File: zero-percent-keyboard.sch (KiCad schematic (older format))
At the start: 195 parts, among them J1 USB4085-GF-A_REVA, SW1 SW_PUSH, U1 ATMEGA32U4, X1 XTAL_GND

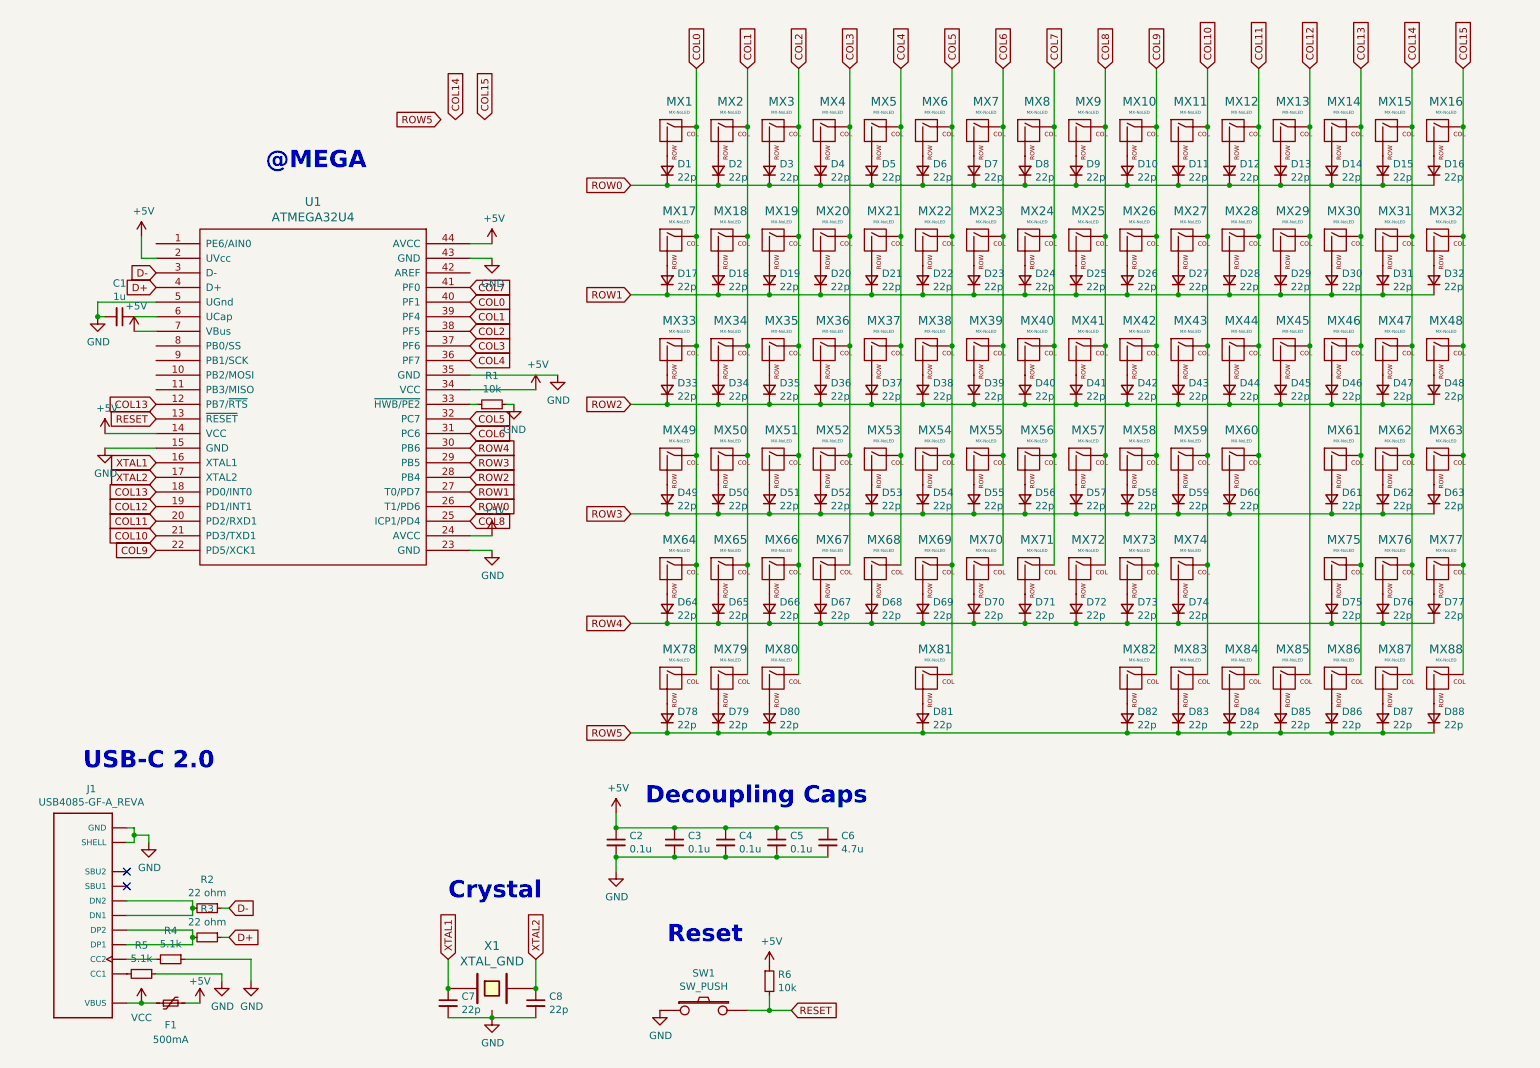
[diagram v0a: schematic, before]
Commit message: Layout change
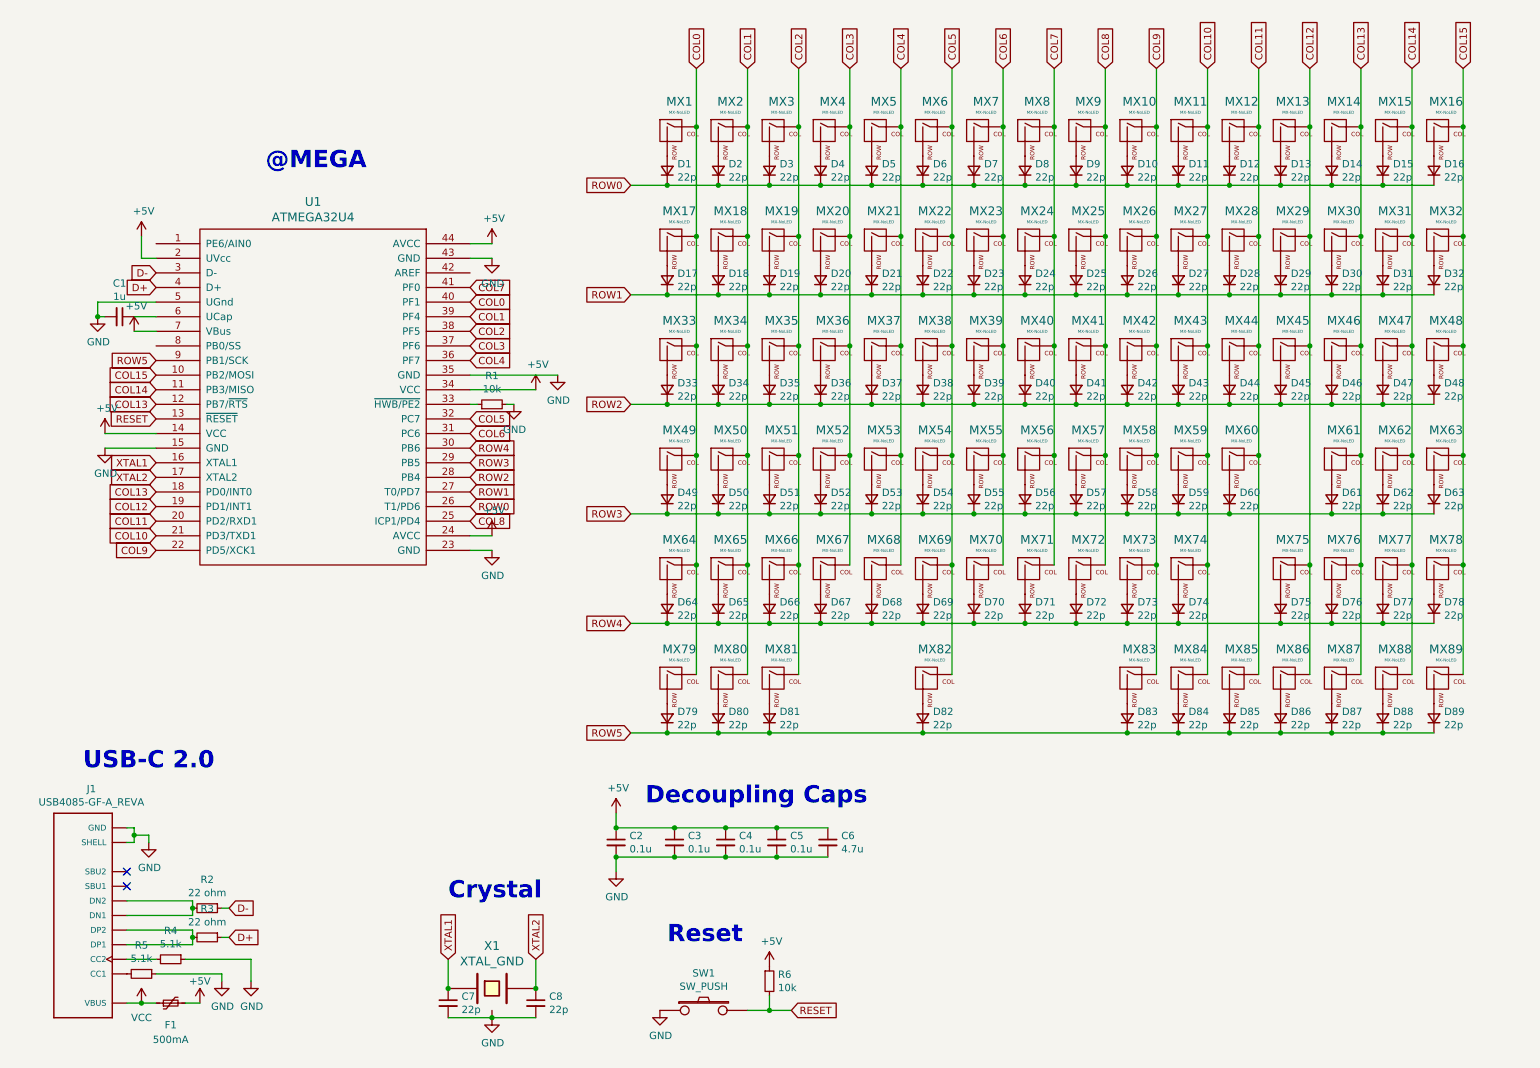
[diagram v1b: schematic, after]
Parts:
- added D75: 22p, Diode_SMD:D_SOD-123, symbol Device:D_Small
- added MX75: MX-NoLED, MX_Only:MXOnly-1.75U-NoLED, symbol MX_Alps_Hybrid:MX-NoLED
- MX17, MX43, MX51, MX52, MX53, MX55, MX56, MX57, MX58, MX65, MX66, MX67, MX68, MX69, MX70, MX71, MX72, MX73, MX74: footprint MX_Only:MXOnly-1.25U-NoLED -> MX_Only:MXOnly-1U-NoLED
- MX28: footprint MX_Only:MXOnly-1.75U-NoLED -> MX_Only:MXOnly-1U-NoLED
- MX30: footprint MX_Only:MXOnly-1U-NoLED -> MX_Only:MXOnly-2U-NoLED
- MX33: footprint MX_Only:MXOnly-1.75U-NoLED -> MX_Only:MXOnly-1.5U-NoLED
- MX46: footprint MX_Only:MXOnly-1U-NoLED -> MX_Only:MXOnly-1.5U-NoLED
- MX49: footprint MX_Only:MXOnly-1.25U-NoLED -> MX_Only:MXOnly-1.75U-NoLED
- MX54: footprint MX_Only:MXOnly-6.25U-ReversedStabilizers-NoLED -> MX_Only:MXOnly-1U-NoLED
- MX61: footprint MX_Only:MXOnly-1U-NoLED -> MX_Only:MXOnly-2.25U-NoLED
- MX64: footprint MX_Only:MXOnly-1.25U-NoLED -> MX_Only:MXOnly-2.25U-NoLED
- MX76: renamed from MX75; footprint MX_Only:MXOnly-1.25U-NoLED -> MX_Only:MXOnly-1U-NoLED
- MX77: renamed from MX76; footprint MX_Only:MXOnly-1.25U-NoLED -> MX_Only:MXOnly-1U-NoLED
- MX78: renamed from MX77; footprint MX_Only:MXOnly-1.25U-NoLED -> MX_Only:MXOnly-1U-NoLED
- MX82: renamed from MX81; footprint MX_Only:MXOnly-1.25U-NoLED -> MX_Only:MXOnly-6.25U-ReversedStabilizers-NoLED
- MX83: renamed from MX82; footprint MX_Only:MXOnly-1.25U-NoLED -> MX_Only:MXOnly-1U-NoLED
- MX84: renamed from MX83; footprint MX_Only:MXOnly-1.25U-NoLED -> MX_Only:MXOnly-1U-NoLED
- MX85: renamed from MX84; footprint MX_Only:MXOnly-1.25U-NoLED -> MX_Only:MXOnly-1U-NoLED
- MX86: renamed from MX85; footprint MX_Only:MXOnly-1.25U-NoLED -> MX_Only:MXOnly-1U-NoLED
- MX87: renamed from MX86; footprint MX_Only:MXOnly-1.25U-NoLED -> MX_Only:MXOnly-1U-NoLED
- MX88: renamed from MX87; footprint MX_Only:MXOnly-1.25U-NoLED -> MX_Only:MXOnly-1U-NoLED
- MX89: renamed from MX88; footprint MX_Only:MXOnly-1.25U-NoLED -> MX_Only:MXOnly-1U-NoLED
- renumbered D75 to D76, D76 to D77, D77 to D78, D78 to D79, D79 to D80, D80 to D81, D81 to D82, D82 to D83, D83 to D84, D84 to D85, D85 to D86, D86 to D87, D87 to D88, D88 to D89, MX78 to MX79, MX79 to MX80, MX80 to MX81
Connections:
- net COL12: now also MX75.1 (COL)
- net COL14: now also U1.11 (PB3/MISO)
- net COL15: now also U1.10 (PB2/MOSI)
- net ROW4: now also D75.1 (K)
- net ROW5: now also U1.9 (PB1/SCK)
- new net: D75.2 (A), MX75.2 (ROW)

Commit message: Route traces
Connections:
- net COL0: now also U1.31 (PC6); no longer U1.40 (PF1)
- net COL1: now also U1.32 (PC7); no longer U1.39 (PF4)
- net COL5: no longer U1.32 (PC7)
- net COL6: no longer U1.31 (PC6)
- net COL8: no longer U1.25 (ICP1/PD4)
- net ROW5: now also U1.25 (ICP1/PD4); no longer U1.9 (PB1/SCK)
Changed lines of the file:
@@
 Text GLabel 3850 2400 2    50   Input ~ 0
 COL7
-Text GLabel 3850 3400 2    50   Input ~ 0
+Text GLabel 4250 2650 2    50   Input ~ 0
 COL6
-Text GLabel 3850 3300 2    50   Input ~ 0
+Text GLabel 4250 2550 2    50   Input ~ 0
 COL5
 Text GLabel 3850 2900 2    50   Input ~ 0
@@
 Text GLabel 3850 3700 2    50   Input ~ 0
 ROW2
-Text GLabel 3850 2600 2    50   Input ~ 0
+Text GLabel 3850 3300 2    50   Input ~ 0
 COL1
-Text GLabel 3850 2500 2    50   Input ~ 0
+Text GLabel 3850 3400 2    50   Input ~ 0
 COL0
-Text GLabel 3850 4000 2    50   Input ~ 0
+Text GLabel 1400 2900 2    50   Input ~ 0
 COL8
 Text GLabel 1700 4200 0    50   Input ~ 0
@@
 Text GLabel 3850 3500 2    50   Input ~ 0
 ROW4
-Text GLabel 1700 2900 0    50   Input ~ 0
+Text GLabel 3850 4000 2    50   Input ~ 0
 ROW5
 $Comp

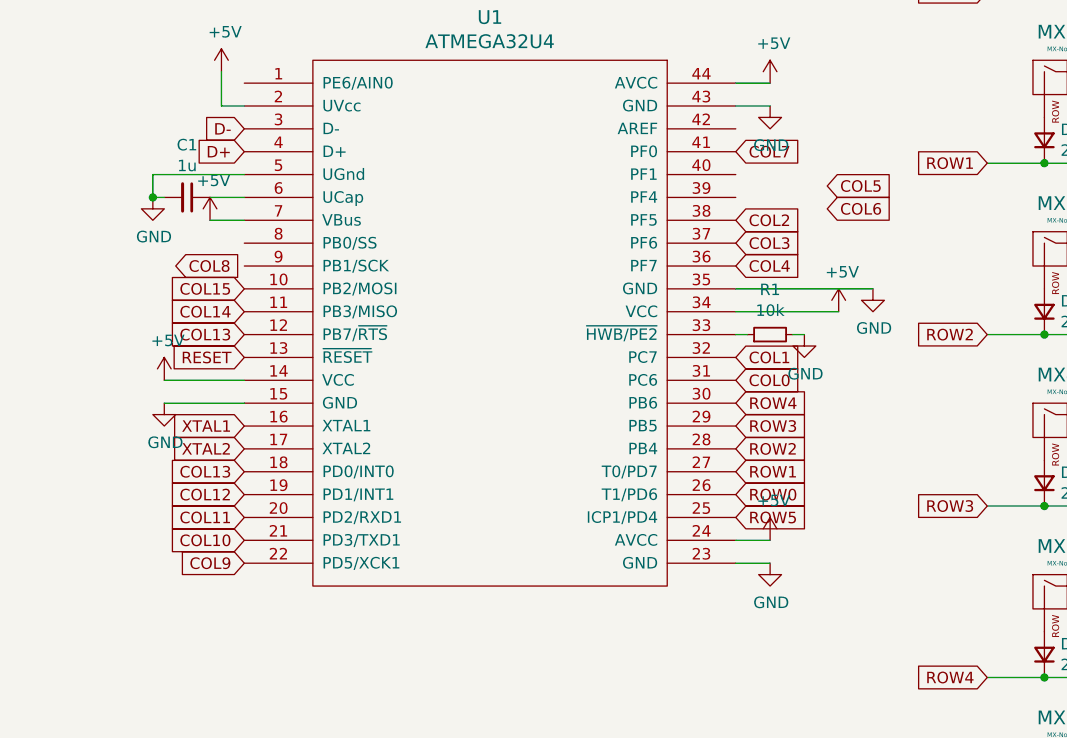
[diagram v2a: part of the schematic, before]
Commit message: Rearrange rows and columns in schematic
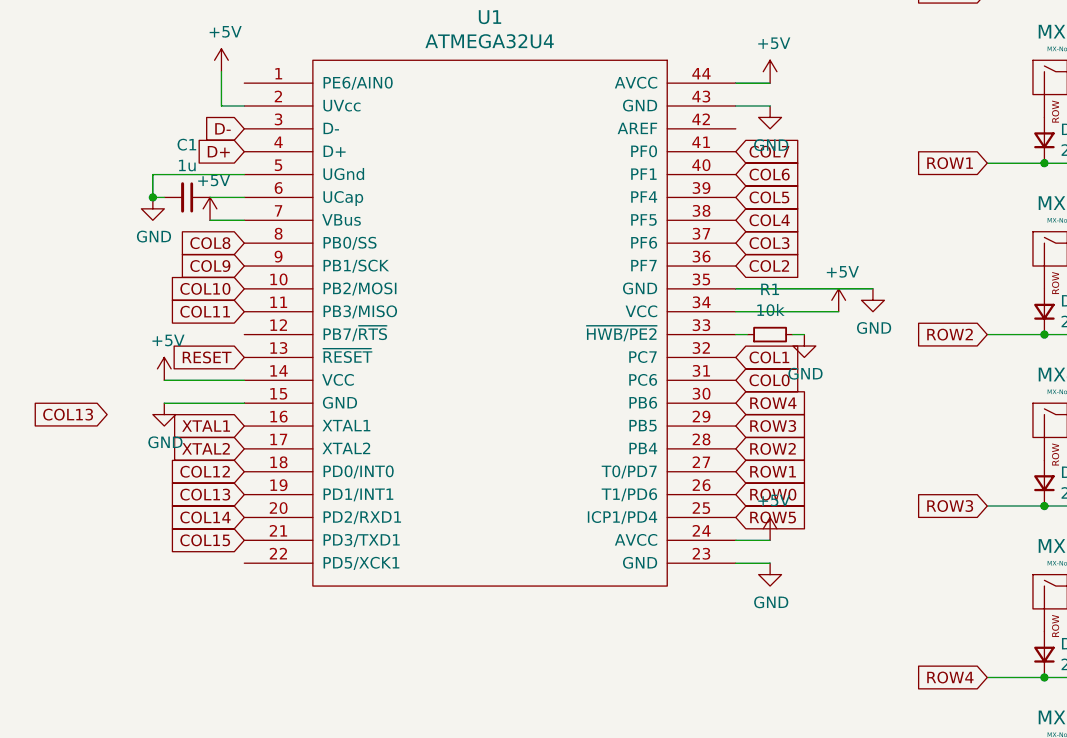
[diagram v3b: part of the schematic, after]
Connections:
- net COL10: now also U1.10 (PB2/MOSI); no longer U1.21 (PD3/TXD1)
- net COL11: now also U1.11 (PB3/MISO); no longer U1.20 (PD2/RXD1)
- net COL12: now also U1.18 (PD0/INT0); no longer U1.19 (PD1/INT1)
- net COL13: now also U1.19 (PD1/INT1); no longer U1.12 (PB7/~RTS), U1.18 (PD0/INT0)
- net COL14: now also U1.20 (PD2/RXD1); no longer U1.11 (PB3/MISO)
- net COL15: now also U1.21 (PD3/TXD1); no longer U1.10 (PB2/MOSI)
- net COL2: now also U1.36 (PF7); no longer U1.38 (PF5)
- net COL4: now also U1.38 (PF5); no longer U1.36 (PF7)
- net COL5: now also U1.39 (PF4)
- net COL6: now also U1.40 (PF1)
- net COL8: now also U1.8 (PB0/SS)
- net COL9: now also U1.9 (PB1/SCK); no longer U1.22 (PD5/XCK1)
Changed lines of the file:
@@
 Text GLabel 3850 2400 2    50   Input ~ 0
 COL7
-Text GLabel 4250 2650 2    50   Input ~ 0
+Text GLabel 3850 2500 2    50   Input ~ 0
 COL6
-Text GLabel 4250 2550 2    50   Input ~ 0
+Text GLabel 3850 2600 2    50   Input ~ 0
 COL5
-Text GLabel 3850 2900 2    50   Input ~ 0
+Text GLabel 3850 2700 2    50   Input ~ 0
 COL4
 Text GLabel 3850 2800 2    50   Input ~ 0
 COL3
-Text GLabel 3850 2700 2    50   Input ~ 0
+Text GLabel 3850 2900 2    50   Input ~ 0
 COL2
 Text GLabel 3850 3700 2    50   Input ~ 0
@@
 Text GLabel 3850 3400 2    50   Input ~ 0
 COL0
-Text GLabel 1400 2900 2    50   Input ~ 0
+Text GLabel 1700 2800 0    50   Input ~ 0
 COL8
-Text GLabel 1700 4200 0    50   Input ~ 0
+Text GLabel 1700 2900 0    50   Input ~ 0
 COL9
-Text GLabel 1700 4100 0    50   Input ~ 0
+Text GLabel 1700 3000 0    50   Input ~ 0
 COL10
-Text GLabel 1700 4000 0    50   Input ~ 0
+Text GLabel 1700 3100 0    50   Input ~ 0
 COL11
-Text GLabel 1700 3900 0    50   Input ~ 0
+Text GLabel 1700 3800 0    50   Input ~ 0
 COL12
-Text GLabel 1700 3200 0    50   Input ~ 0
+Text GLabel 1100 3550 0    50   Input ~ 0
 COL13
 $Comp
@@
 Text GLabel 10300 900  1    50   Input ~ 0
 COL14
-Text GLabel 1700 3800 0    50   Input ~ 0
+Text GLabel 1700 3900 0    50   Input ~ 0
 COL13
-Text GLabel 1700 3100 0    50   Input ~ 0
+Text GLabel 1700 4000 0    50   Input ~ 0
 COL14
-Text GLabel 1700 3000 0    50   Input ~ 0
+Text GLabel 1700 4100 0    50   Input ~ 0
 COL15
 Text GLabel 3850 3500 2    50   Input ~ 0

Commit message: Add Title
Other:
- note added: "1"
- note added: "November 2020"
- note added: "Zero Percent Keyboard"
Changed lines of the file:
@@
 Wire Wire Line
 	9400 4700 9750 4700
+Text Notes 7000 7000 0    197  ~ 39
+Zero Percent Keyboard
+Text Notes 8100 7650 0    59   ~ 12
+November 2020
+Text Notes 10600 7650 0    59   ~ 12
+1
+Text Notes 7350 7500 0    79   ~ 16
+Zero Percent Keyboard
 $EndSCHEMATC
